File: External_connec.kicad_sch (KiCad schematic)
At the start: 16 parts, among them CN1 JST_Battery, J11 CAN_TX, J12 CAN_RX, J13 Conn_01x08, J14 Conn_01x06, J15 Conn_01x10, J16 Conn_01x08, J2 A - B, J21 U2U, J3 H - L, J4 TYPE-C-31-M12_13, J5 EXT_LOAD, J9 Conn_01x06

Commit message: Finished routing
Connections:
- net CAN_RX/GPIO8: now also J15.2 (Pin_2); no longer J13.7 (Pin_7)
- net CAN_TX/GPIO7: now also J15.1 (Pin_1); no longer J13.8 (Pin_8)
- net GPIO14: now also J13.7 (Pin_7); no longer J15.2 (Pin_2)
- net GPIO9: now also J13.8 (Pin_8); no longer J15.1 (Pin_1)
- net GPIO33 renamed GPIO46
- net GPIO34 renamed GPIO45
- net RS-485_RX/GPIO46 renamed RS-485_TX/GPIO33
- net RS-485_TX/GPIO45 renamed RS-485_RX/GPIO34
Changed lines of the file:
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@@
     (effects (font (size 1.27 1.27) bold (color 132 132 0 1)) (justify left bottom))
   )
-  (label "GPIO34" (at 123.825 168.91 180) (fields_autoplaced)
+  (label "GPIO46" (at 123.825 168.91 180) (fields_autoplaced)
     (effects (font (size 1.27 1.27) bold (color 72 0 0 1)) (justify right bottom))
   )
@@
     (effects (font (size 1.27 1.27) bold (color 255 0 0 1)) (justify right bottom))
   )
-  (label "CAN_TX{slash}GPIO7" (at 197.485 66.675 180) (fields_autoplaced)
+  (label "CAN_TX{slash}GPIO7" (at 197.485 62.23 180) (fields_autoplaced)
     (effects (font (size 1.27 1.27) bold (color 0 0 255 1)) (justify right bottom))
   )
@@
     (effects (font (size 1.27 1.27) bold (color 72 0 0 1)) (justify right bottom))
   )
-  (label "RS-485_TX{slash}GPIO45" (at 133.985 189.23 180) (fields_autoplaced)
+  (label "RS-485_TX{slash}GPIO33" (at 133.985 189.23 180) (fields_autoplaced)
     (effects (font (size 1.27 1.27) bold (color 0 0 255 1)) (justify right bottom))
   )
@@
     (effects (font (size 1.27 1.27) bold (color 0 0 255 1)) (justify left bottom))
   )
-  (label "RS-485_RX{slash}GPIO46" (at 127 31.75 0) (fields_autoplaced)
-    (effects (font (size 1.27 1.27) bold (color 0 0 255 1)) (justify left bottom))
-  )
-  (label "GPIO33" (at 123.825 166.37 180) (fields_autoplaced)
+  (label "RS-485_RX{slash}GPIO34" (at 127 34.29 0) (fields_autoplaced)
+    (effects (font (size 1.27 1.27) bold (color 0 0 255 1)) (justify left bottom))
+  )
+  (label "GPIO45" (at 123.825 166.37 180) (fields_autoplaced)
     (effects (font (size 1.27 1.27) bold (color 72 0 0 1)) (justify right bottom))
   )
@@
     (effects (font (size 1.27 1.27) bold (color 72 0 0 1)) (justify left bottom))
   )
-  (label "GPIO9" (at 197.485 62.23 180) (fields_autoplaced)
+  (label "GPIO9" (at 197.485 66.675 180) (fields_autoplaced)
     (effects (font (size 1.27 1.27) bold (color 72 0 0 1)) (justify right bottom))
   )
@@
     (effects (font (size 1.27 1.27) bold (color 0 0 255 1)) (justify right bottom))
   )
-  (label "RS-485_TX{slash}GPIO45" (at 127 34.29 0) (fields_autoplaced)
+  (label "RS-485_TX{slash}GPIO33" (at 127 31.75 0) (fields_autoplaced)
     (effects (font (size 1.27 1.27) bold (color 0 0 255 1)) (justify left bottom))
   )
@@
     (effects (font (size 1.27 1.27) bold (color 72 0 0 1)) (justify right bottom))
   )
-  (label "GPIO34" (at 197.485 79.375 180) (fields_autoplaced)
-    (effects (font (size 1.27 1.27) bold (color 72 0 0 1)) (justify right bottom))
-  )
-  (label "CAN_RX{slash}GPIO8" (at 197.485 69.215 180) (fields_autoplaced)
+  (label "GPIO46" (at 197.485 81.915 180) (fields_autoplaced)
+    (effects (font (size 1.27 1.27) bold (color 72 0 0 1)) (justify right bottom))
+  )
+  (label "CAN_RX{slash}GPIO8" (at 197.485 59.69 180) (fields_autoplaced)
     (effects (font (size 1.27 1.27) bold (color 0 0 255 1)) (justify right bottom))
   )
@@
     (effects (font (size 1.27 1.27) bold (color 72 0 0 1)) (justify right bottom))
   )
-  (label "RS-485_TX{slash}GPIO46" (at 133.985 191.77 180) (fields_autoplaced)
+  (label "RS-485_RX{slash}GPIO34" (at 133.985 191.77 180) (fields_autoplaced)
     (effects (font (size 1.27 1.27) bold (color 0 0 255 1)) (justify right bottom))
   )
@@
     (effects (font (size 1.27 1.27) bold (color 0 194 0 1)) (justify left bottom))
   )
-  (label "GPIO33" (at 197.485 81.915 180) (fields_autoplaced)
+  (label "GPIO45" (at 197.485 79.375 180) (fields_autoplaced)
     (effects (font (size 1.27 1.27) bold (color 72 0 0 1)) (justify right bottom))
   )
@@
     (effects (font (size 1.27 1.27) bold (color 72 0 0 1)) (justify right bottom))
   )
-  (label "GPIO14" (at 197.485 59.69 180) (fields_autoplaced)
+  (label "GPIO14" (at 197.485 69.215 180) (fields_autoplaced)
     (effects (font (size 1.27 1.27) bold (color 72 0 0 1)) (justify right bottom))
   )
@@
     (effects (font (size 1.27 1.27) (thickness 0.254) bold (color 72 0 72 1)) (justify right))
   )
-  (hierarchical_label "GPIO33" (shape input) (at 114.3 166.37 180) (fields_autoplaced)
-    (effects (font (size 1.27 1.27) (thickness 0.254) bold (color 72 0 72 1)) (justify right))
-  )
-  (hierarchical_label "GPIO34" (shape input) (at 114.3 168.91 180) (fields_autoplaced)
+  (hierarchical_label "GPIO45" (shape input) (at 114.3 166.37 180) (fields_autoplaced)
+    (effects (font (size 1.27 1.27) (thickness 0.254) bold (color 72 0 72 1)) (justify right))
+  )
+  (hierarchical_label "GPIO46" (shape input) (at 114.3 168.91 180) (fields_autoplaced)
     (effects (font (size 1.27 1.27) (thickness 0.254) bold (color 72 0 72 1)) (justify right))
   )
@@
     (effects (font (size 1.27 1.27) (thickness 0.254) bold (color 72 0 72 1)) (justify right))
   )
-  (hierarchical_label "RS-485_RX{slash}GPIO46" (shape input) (at 114.3 191.77 180) (fields_autoplaced)
+  (hierarchical_label "RS-485_RX{slash}GPIO34" (shape input) (at 114.3 191.77 180) (fields_autoplaced)
     (effects (font (size 1.27 1.27) (thickness 0.254) bold (color 0 0 255 1)) (justify right))
   )
-  (hierarchical_label "RS-485_TX{slash}GPIO45" (shape input) (at 114.3 189.23 180) (fields_autoplaced)
+  (hierarchical_label "RS-485_TX{slash}GPIO33" (shape input) (at 114.3 189.23 180) (fields_autoplaced)
     (effects (font (size 1.27 1.27) (thickness 0.254) bold (color 0 0 255 1)) (justify right))
   )

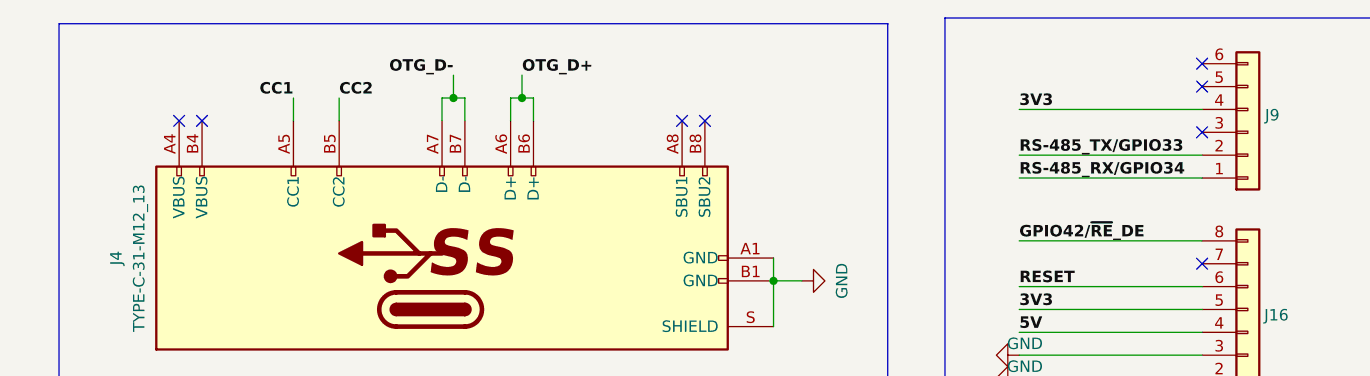
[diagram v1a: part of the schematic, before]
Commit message: Added GND vias along antenna track, cleared tracks underneath antenna track
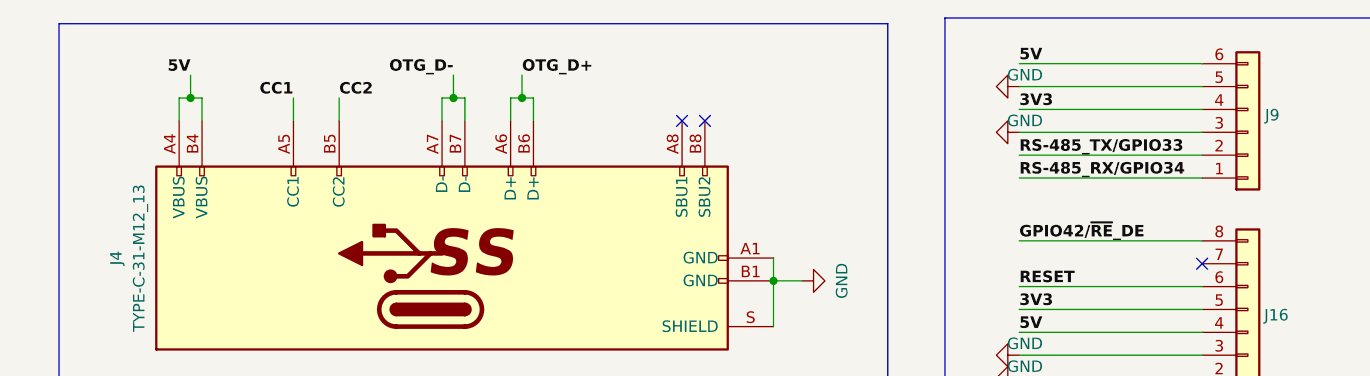
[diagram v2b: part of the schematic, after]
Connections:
- net 5V: now also J4.A4 (VBUS), J4.B4 (VBUS), J9.6 (Pin_6)
- net GND: now also J9.3 (Pin_3), J9.5 (Pin_5)
- no-connect marks 12 -> 7
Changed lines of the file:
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@@
   (junction (at 99.695 45.72) (diameter 0) (color 0 0 0 0)
   )
+  (junction (at 34.925 25.4) (diameter 0) (color 0 0 0 0)
+  )
   (junction (at 64.135 25.4) (diameter 0) (color 0 0 0 0)
   )
   (junction (at 71.755 25.4) (diameter 0) (color 0 0 0 0)
   )
-  (no_connect (at 147.32 24.13))
   (no_connect (at 147.32 59.055))
   (no_connect (at 92.075 27.94))
-  (no_connect (at 33.655 27.94))
   (no_connect (at 252.095 98.425))
   (no_connect (at 177.165 57.15))
-  (no_connect (at 147.32 29.21))
-  (no_connect (at 147.32 21.59))
   (no_connect (at 89.535 27.94))
   (no_connect (at 147.32 43.815))
   (no_connect (at 239.395 98.425))
-  (no_connect (at 36.195 27.94))
   (wire (pts (xy 97.155 186.69) (xy 87.63 186.69))
     (stroke (width 0.5) (type default) (color 72 0 0 1))
@@
     (stroke (width 1) (type default) (color 72 72 72 1))
   )
+  (wire (pts (xy 33.655 25.4) (xy 34.925 25.4))
+    (stroke (width 0) (type default))
+  )
   (wire (pts (xy 154.305 177.8) (xy 144.78 177.8))
     (stroke (width 0.5) (type default) (color 0 194 0 1))
@@
     (stroke (width 1) (type default) (color 72 72 72 1))
   )
+  (wire (pts (xy 127 21.59) (xy 147.32 21.59))
+    (stroke (width 0) (type default))
+  )
   (wire (pts (xy 197.485 54.61) (xy 177.165 54.61))
     (stroke (width 0) (type default))
@@
     (stroke (width 1) (type default) (color 72 72 72 1))
   )
+  (wire (pts (xy 34.925 25.4) (xy 36.195 25.4))
+    (stroke (width 0) (type default))
+  )
   (wire (pts (xy 197.485 62.23) (xy 177.165 62.23))
     (stroke (width 0) (type default))
@@
     (stroke (width 1) (type default) (color 72 72 72 1))
   )
+  (wire (pts (xy 127 24.13) (xy 147.32 24.13))
+    (stroke (width 0) (type default))
+  )
   (bus (pts (xy 212.09 123.19) (xy 212.09 139.7))
     (stroke (width 1) (type default) (color 72 72 72 1))
@@
   (wire (pts (xy 159.385 160.02) (xy 144.78 160.02))
     (stroke (width 0.5) (type default) (color 72 0 0 1))
+  )
+  (wire (pts (xy 34.925 22.86) (xy 34.925 25.4))
+    (stroke (width 0) (type default))
   )
   (wire (pts (xy 69.215 176.53) (xy 53.34 176.53))
     (stroke (width 0.5) (type default) (color 0 0 0 1))
   )
+  (wire (pts (xy 36.195 25.4) (xy 36.195 27.94))
+    (stroke (width 0) (type default))
+  )
   (wire (pts (xy 133.985 189.23) (xy 114.3 189.23))
     (stroke (width 0.5) (type default) (color 0 0 255 1))
@@
     (stroke (width 1) (type default) (color 72 72 72 1))
   )
+  (wire (pts (xy 127 29.21) (xy 147.32 29.21))
+    (stroke (width 0) (type default))
+  )
   (wire (pts (xy 86.36 76.2) (xy 86.36 72.39))
     (stroke (width 0) (type default))
@@
     (stroke (width 1) (type default) (color 72 72 72 1))
   )
+  (wire (pts (xy 33.655 25.4) (xy 33.655 27.94))
+    (stroke (width 0) (type default))
+  )
   (wire (pts (xy 197.485 44.45) (xy 177.165 44.45))
     (stroke (width 0) (type default))
@@
     (effects (font (size 1.27 1.27) bold (color 0 0 0 1)) (justify left bottom))
   )
+  (label "5V" (at 127 21.59 0) (fields_autoplaced)
+    (effects (font (size 1.27 1.27) bold (color 255 0 0 1)) (justify left bottom))
+  )
   (label "V_BAT" (at 250.19 92.075 0) (fields_autoplaced)
     (effects (font (size 1.27 1.27) bold (color 132 132 0 1)) (justify left bottom))
@@
   (label "RS-485_TX{slash}GPIO33" (at 133.985 189.23 180) (fields_autoplaced)
     (effects (font (size 1.27 1.27) bold (color 0 0 255 1)) (justify right bottom))
+  )
+  (label "5V" (at 34.925 22.86 180) (fields_autoplaced)
+    (effects (font (size 1.27 1.27) bold (color 255 0 0 1)) (justify right bottom))
   )
   (label "GPIO39" (at 123.825 181.61 180) (fields_autoplaced)
@@
     )
   )
+  (symbol (lib_id "ESP32-S3_DB:GND") (at 127 29.21 270) (unit 1)
+    (in_bom yes) (on_board yes) (dnp no)
+    (property "Reference" "#PWR066" (at 120.65 29.21 0)
+      (effects (font (size 1.27 1.27)) hide)
+    )
+    (property "Value" "GND" (at 127.635 27.94 90)
+      (effects (font (size 1.27 1.27)))
+    )
+    (property "Footprint" "" (at 127 29.21 0)
+      (effects (font (size 1.27 1.27)) hide)
+    )
+    (property "Datasheet" "" (at 127 29.21 0)
+      (effects (font (size 1.27 1.27)) hide)
+    )
+    (pin "1")
+    (instances
+      (project "ESP32-S3_DB"
+        (path "/b7fc4bd3-c219-4455-832b-8d795385dcf1/e2721808-ce0b-4b73-8382-0fd911e1c931"
+          (reference "#PWR066") (unit 1)
+        )
+      )
+    )
+  )
   (symbol (lib_id "ESP32-S3_DB:Screw_Terminal_01x03") (at 48.26 132.08 0) (unit 1)
     (in_bom yes) (on_board yes) (dnp no)
@@
         )
       )
+    )
+  )
+  (symbol (lib_id "ESP32-S3_DB:GND") (at 127 24.13 270) (unit 1)
+    (in_bom yes) (on_board yes) (dnp no)
+    (property "Reference" "#PWR072" (at 120.65 24.13 0)
+      (effects (font (size 1.27 1.27)) hide)
+    )
+    (property "Value" "GND" (at 127.635 22.86 90)
+      (effects (font (size 1.27 1.27)))
+    )
+    (property "Footprint" "" (at 127 24.13 0)
+      (effects (font (size 1.27 1.27)) hide)
+    )
+    (property "Datasheet" "" (at 127 24.13 0)
+      (effects (font (size 1.27 1.27)) hide)
+    )
+    (pin "1")
+    (instances
+      (project "ESP32-S3_DB"
+        (path "/b7fc4bd3-c219-4455-832b-8d795385dcf1/e2721808-ce0b-4b73-8382-0fd911e1c931"
+          (reference "#PWR072") (unit 1)
+        )
+      )

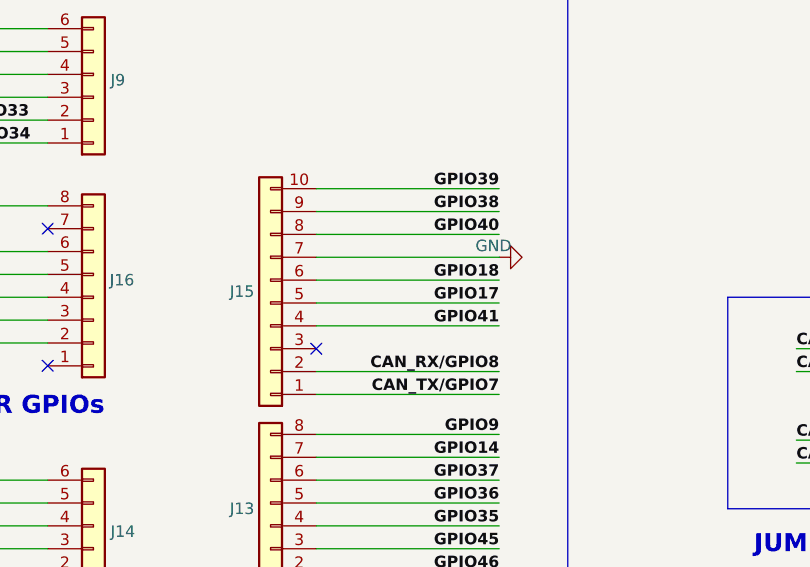
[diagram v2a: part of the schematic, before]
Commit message: Added Arduino style SS for GPIO headers, Added BLE & Wi-Fi symbol
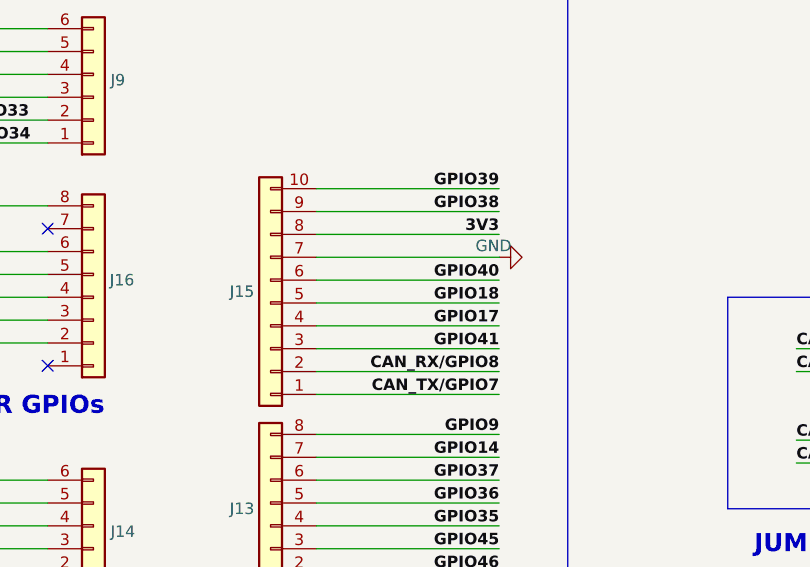
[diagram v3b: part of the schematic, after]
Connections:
- net 3V3: now also J15.8 (Pin_8)
- net GPIO17: now also J15.4 (Pin_4); no longer J15.5 (Pin_5)
- net GPIO18: now also J15.5 (Pin_5); no longer J15.6 (Pin_6)
- net GPIO40: now also J15.6 (Pin_6); no longer J15.8 (Pin_8)
- net GPIO41: now also J15.3 (Pin_3); no longer J15.4 (Pin_4)
- no-connect marks 7 -> 6
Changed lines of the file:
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@@
   (no_connect (at 92.075 27.94))
   (no_connect (at 252.095 98.425))
-  (no_connect (at 177.165 57.15))
   (no_connect (at 89.535 27.94))
   (no_connect (at 147.32 43.815))
@@
     (stroke (width 0.5) (type default) (color 72 0 0 1))
   )
+  (wire (pts (xy 197.485 57.15) (xy 177.165 57.15))
+    (stroke (width 0) (type default))
+  )
   (bus (pts (xy 222.885 51.435) (xy 222.885 74.93))
     (stroke (width 1) (type default) (color 72 72 72 1))
@@
     (effects (font (size 1.27 1.27) bold (color 72 0 0 1)) (justify right bottom))
   )
-  (label "GPIO17" (at 197.485 52.07 180) (fields_autoplaced)
+  (label "GPIO17" (at 197.485 54.61 180) (fields_autoplaced)
     (effects (font (size 1.27 1.27) bold (color 72 0 0 1)) (justify right bottom))
   )
@@
     (effects (font (size 1.27 1.27) bold (color 0 0 255 1)) (justify right bottom))
   )
-  (label "GPIO18" (at 197.485 49.53 180) (fields_autoplaced)
+  (label "GPIO18" (at 197.485 52.07 180) (fields_autoplaced)
     (effects (font (size 1.27 1.27) bold (color 72 0 0 1)) (justify right bottom))
   )
@@
     (effects (font (size 1.27 1.27) bold (color 72 0 0 1)) (justify right bottom))
   )
+  (label "GPIO41" (at 197.485 57.15 180) (fields_autoplaced)
+    (effects (font (size 1.27 1.27) bold (color 72 0 0 1)) (justify right bottom))
+  )
   (label "GPIO35" (at 197.485 76.835 180) (fields_autoplaced)
     (effects (font (size 1.27 1.27) bold (color 72 0 0 1)) (justify right bottom))
@@
     (effects (font (size 1.27 1.27) bold (color 72 0 0 1)) (justify right bottom))
   )
+  (label "3V3" (at 197.485 44.45 180) (fields_autoplaced)
+    (effects (font (size 1.27 1.27) bold (color 255 0 0 1)) (justify right bottom))
+  )
   (label "CAN_TRANS_TXD" (at 230.505 59.69 0) (fields_autoplaced)
     (effects (font (size 1.27 1.27) (thickness 0.254) bold (color 0 0 255 1)) (justify left bottom))
@@
     (effects (font (size 1.27 1.27) bold (color 0 0 0 1)) (justify right bottom))
   )
-  (label "GPIO40" (at 197.485 44.45 180) (fields_autoplaced)
+  (label "GPIO40" (at 197.485 49.53 180) (fields_autoplaced)
     (effects (font (size 1.27 1.27) bold (color 72 0 0 1)) (justify right bottom))
   )
@@
     (effects (font (size 1.27 1.27) bold (color 72 0 0 1)) (justify left bottom))
   )
-  (label "GPIO41" (at 197.485 54.61 180) (fields_autoplaced)
-    (effects (font (size 1.27 1.27) bold (color 72 0 0 1)) (justify right bottom))
-  )
   (label "GPIO17" (at 97.155 186.69 180) (fields_autoplaced)
